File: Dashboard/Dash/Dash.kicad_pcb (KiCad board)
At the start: 2 copper layers, 184 x 75 mm, 43 parts, among them IC1 MCP25625-E_SS, J1 TACH-SERVO, J2 SPEED-SERVO, J6 LOWER Button, J7 DTF13-6P, U1 XIAO-ESP32-S3-SMD, U3 EA DOGM128W-6, Y1 ABM10AIG-16.000MHZ-4Z-T3

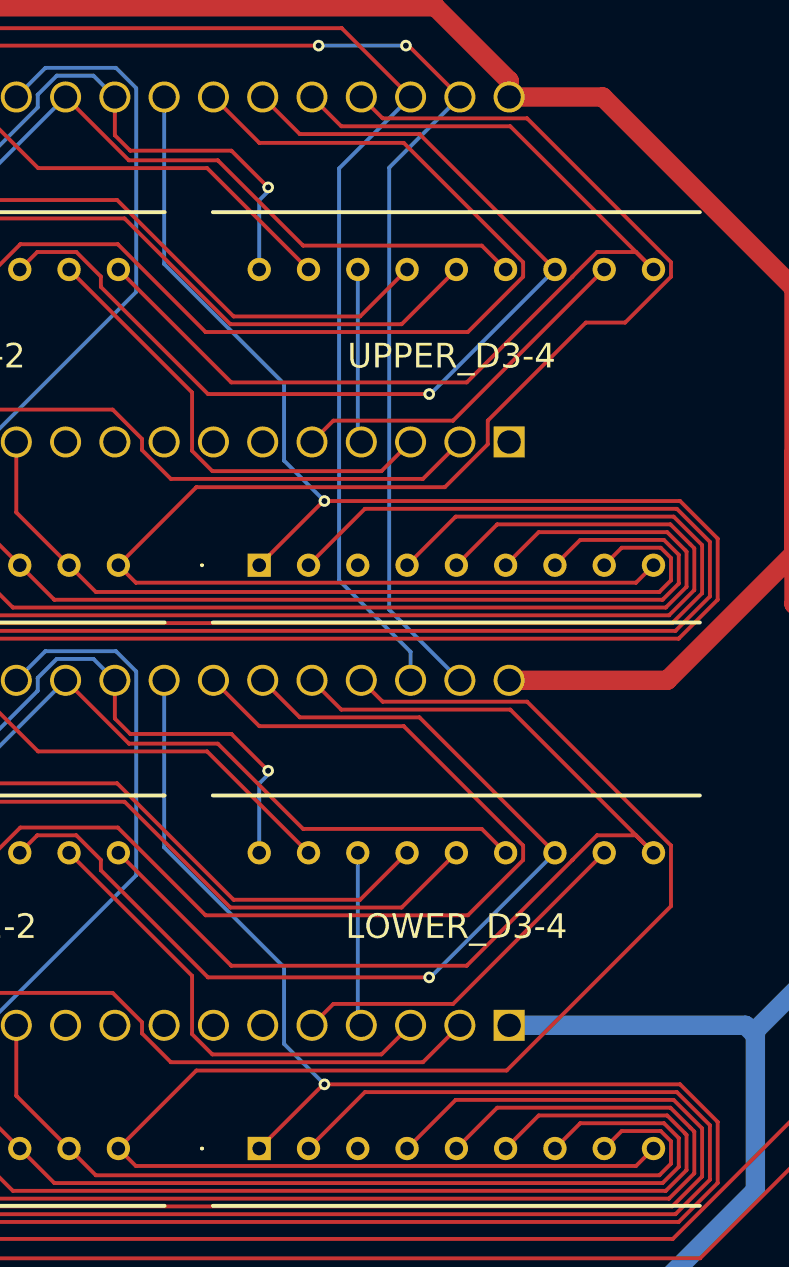
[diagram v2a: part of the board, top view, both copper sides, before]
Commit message: Fixed Shorting DRC Errors
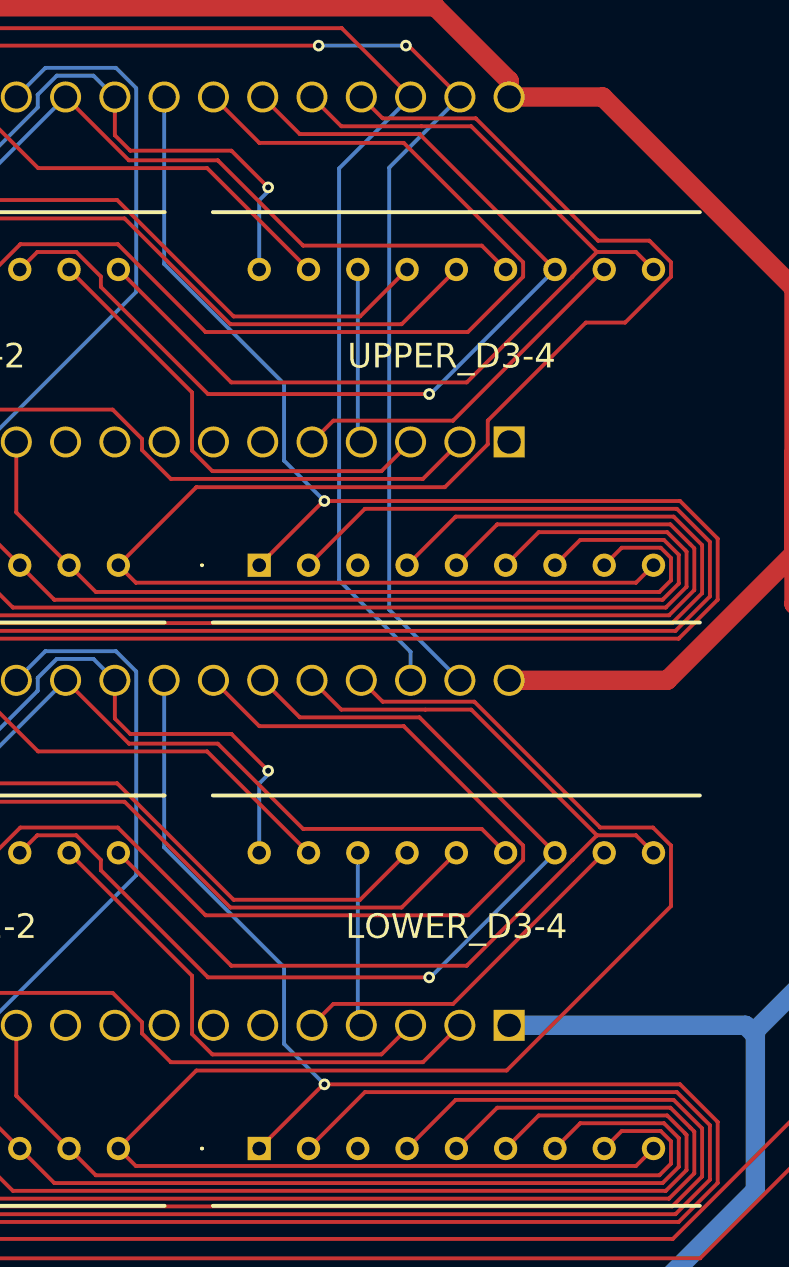
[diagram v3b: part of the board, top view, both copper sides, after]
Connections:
- LOWER_D1-2 pad 8: ROW14_UPPER -> ROW14_LOWER
- LOWER_D3-4 pad 8: ROW14_UPPER -> ROW14_LOWER
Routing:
- net ROW14_LOWER: track 0.00 -> 44.5 mm
- net (no net): track 44.5 -> 0.00 mm
- net ROW1_UPPER: track 54.4 -> 51.1 mm
- net ROW1_LOWER: track 54.4 -> 51.1 mm
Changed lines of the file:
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@@
 			(layers "*.Cu" "*.Mask")
 			(remove_unused_layers no)
-			(net 3 "ROW14_UPPER")
+			(net 15 "ROW14_LOWER")
 			(pinfunction "A_DP")
 			(pintype "passive")
@@
 			(layers "*.Cu" "*.Mask")
 			(remove_unused_layers no)
-			(net 3 "ROW14_UPPER")
+			(net 15 "ROW14_LOWER")
 			(pinfunction "A_DP")
 			(pintype "passive")
@@
 	)
 	(segment
-		(start 181.020325 125.22)
-		(end 210.061325 125.22)
-		(width 0.2)
-		(layer "F.Cu")
-		(net 0)
-	)
-	(segment
-		(start 208.121325 122.939)
-		(end 207.220325 123.84)
-		(width 0.2)
-		(layer "F.Cu")
-		(net 0)
-	)
-	(segment
-		(start 176.920325 117.49)
-		(end 176.920325 121.12)
-		(width 0.2)
-		(layer "F.Cu")
-		(net 0)
-	)
-	(segment
-		(start 176.920325 121.12)
-		(end 181.020325 125.22)
-		(width 0.2)
-		(layer "F.Cu")
-		(net 0)
-	)
-	(segment
-		(start 210.661325 124.62)
-		(end 210.661325 123.466793)
-		(width 0.2)
-		(layer "F.Cu")
-		(net 0)
-	)
-	(segment
-		(start 210.661325 123.466793)
-		(end 210.133532 122.939)
-		(width 0.2)
-		(layer "F.Cu")
-		(net 0)
-	)
-	(segment
-		(start 210.133532 122.939)
-		(end 208.121325 122.939)
-		(width 0.2)
-		(layer "F.Cu")
-		(net 0)
-	)
-	(segment
-		(start 210.061325 125.22)
-		(end 210.661325 124.62)
-		(width 0.2)
-		(layer "F.Cu")
-		(net 0)
-	)
-	(segment
 		(start 181.020325 95.157844)
 		(end 210.061325 95.157844)
@@
 	)
 	(segment
-		(start 193.670325 101.22)
-		(end 202.380325 101.22)
+		(start 209.760325 108.599999)
+		(end 209.760325 108.6)
 		(width 0.2)
 		(layer "F.Cu")
@@
 	)
 	(segment
-		(start 202.380325 101.22)
-		(end 209.760325 108.6)
+		(start 200.134532 114.42)
+		(end 188.000325 114.42)
 		(width 0.2)
 		(layer "F.Cu")
@@
 	)
 	(segment
-		(start 200.134532 114.42)
-		(end 188.000325 114.42)
+		(start 200.368118 101.22)
+		(end 206.847118 107.699)
 		(width 0.2)
 		(layer "F.Cu")
@@
 	)
 	(segment
+		(start 198 101.22)
+		(end 200.368118 101.22)
+		(width 0.2)
+		(layer "F.Cu")
+		(net 7)
+	)
+	(segment
 		(start 192.160325 99.71)
 		(end 193.670325 101.22)
@@
 	)
 	(segment
+		(start 193.670325 101.22)
+		(end 198 101.22)
+		(width 0.2)
+		(layer "F.Cu")
+		(net 7)
+	)
+	(segment
 		(start 183.400325 117.90705)
 		(end 183.400325 117.33295)
@@
 	)
 	(segment
+		(start 181.020325 125.22)
+		(end 210.061325 125.22)
+		(width 0.2)
+		(layer "F.Cu")
+		(net 15)
+	)
+	(segment
+		(start 176.920325 117.49)
+		(end 176.920325 121.12)
+		(width 0.2)
+		(layer "F.Cu")
+		(net 15)
+	)
+	(segment
+		(start 176.920325 121.12)
+		(end 181.020325 125.22)
+		(width 0.2)
+		(layer "F.Cu")
+		(net 15)
+	)
+	(segment
+		(start 210.661325 124.62)
+		(end 210.661325 123.466793)
+		(width 0.2)
+		(layer "F.Cu")
+		(net 15)
+	)
+	(segment
+		(start 210.661325 123.466793)
+		(end 210.133532 122.939)
+		(width 0.2)
+		(layer "F.Cu")
+		(net 15)
+	)
+	(segment
+		(start 208.121325 122.939)
+		(end 207.220325 123.84)
+		(width 0.2)
+		(layer "F.Cu")
+		(net 15)
+	)
+	(segment
+		(start 210.133532 122.939)
+		(end 208.121325 122.939)
+		(width 0.2)
+		(layer "F.Cu")
+		(net 15)
+	)
+	(segment
+		(start 210.061325 125.22)
+		(end 210.661325 124.62)
+		(width 0.2)
+		(layer "F.Cu")
+		(net 15)
+	)
+	(segment
 		(start 207.220325 108.6)
 		(end 199.431325 116.389)
@@
 	)
 	(segment
-		(start 210.661325 111.351)
+		(start 209.732532 107.298)
 		(end 210.661325 108.226793)
 		(width 0.2)
@@
 	)
 	(segment
-		(start 202.192325 119.82)
-		(end 210.661325 111.351)
+		(start 194.700325 99.71)
+		(end 195.801325 100.811)
 		(width 0.2)
 		(layer "F.Cu")
@@
 	)
 	(segment
-		(start 186.200325 119.82)
+		(start 195.801325 100.811)
+		(end 200.526218 100.811)
+		(width 0.2)
+		(layer "F.Cu")
+		(net 44)
+	)
+	(segment
+		(start 210.661325 111.351)
 		(end 202.192325 119.82)
 		(width 0.2)
@@
 	)
 	(segment
-		(start 203.245532 100.811)
-		(end 195.801325 100.811)
+		(start 210.661325 108.226793)
+		(end 210.661325 111.351)
 		(width 0.2)
 		(layer "F.Cu")
@@
 	)
 	(segment
-		(start 182.180325 123.84)
-		(end 186.200325 119.82)
+		(start 207.013218 107.298)
+		(end 209.732532 107.298)
 		(width 0.2)
 		(layer "F.Cu")
@@
 	)
 	(segment
-		(start 208.859325 124.741)
-		(end 209.760325 123.84)
+		(start 186.200325 119.82)
+		(end 182.180325 123.84)
 		(width 0.2)
 		(layer "F.Cu")
@@
 	)
 	(segment
-		(start 195.801325 100.811)
-		(end 194.700325 99.71)
+		(start 202.192325 119.82)
+		(end 186.200325 119.82)
 		(width 0.2)
 		(layer "F.Cu")
@@
 	)
 	(segment
-		(start 182.180325 123.84)
-		(end 183.081325 124.741)
+		(start 208.859325 124.741)
+		(end 209.760325 123.84)
 		(width 0.2)
 		(layer "F.Cu")
@@
 	)
 	(segment
-		(start 210.661325 108.226793)
-		(end 203.245532 100.811)
+		(start 200.526218 100.811)
+		(end 207.013218 107.298)
+		(width 0.2)
+		(layer "F.Cu")
+		(net 44)
+	)
+	(segment
+		(start 182.180325 123.84)
+		(end 183.081325 124.741)
 		(width 0.2)
 		(layer "F.Cu")
@@
 	(segment
 		(start 210.661325 78.164637)
-		(end 203.245532 70.748844)
+		(end 209.548344 77.051656)
+		(width 0.2)
+		(layer "F.Cu")
+		(net 85)
+	)
+	(segment
+		(start 209.548344 77.051656)
+		(end 206.902812 77.051656)
 		(width 0.2)
 		(layer "F.Cu")
@@
 	)
 	(segment
-		(start 203.245532 70.748844)
+		(start 200.6 70.748844)
 		(end 195.801325 70.748844)
 		(width 0.2)
@@
 	)
 	(segment
+		(start 206.902812 77.051656)
+		(end 200.6 70.748844)
+		(width 0.2)
+		(layer "F.Cu")
+		(net 85)
+	)
+	(segment
 		(start 201.219325 86.326844)
 		(end 206.273084 81.273084)
@@
 	)
 	(segment
-		(start 202.380325 71.157844)
-		(end 209.760325 78.537844)
-		(width 0.2)
-		(layer "F.Cu")
-		(net 101)
-	)
-	(segment
 		(start 188.000325 84.357844)
 		(end 182.180325 78.537844)
@@
 	)
 	(segment
+		(start 200.368118 71.157844)
+		(end 206.847118 77.636844)
+		(width 0.2)
+		(layer "F.Cu")
+		(net 101)
+	)
+	(segment
+		(start 197.8 71.157844)
+		(end 200.368118 71.157844)
+		(width 0.2)
+		(layer "F.Cu")
+		(net 101)
+	)
+	(segment
 		(start 205.581325 78.902637)
 		(end 205.581325 78.911051)
@@
 	(segment
 		(start 193.670325 71.157844)
-		(end 202.380325 71.157844)
+		(end 197.8 71.157844)
 		(width 0.2)
 		(layer "F.Cu")

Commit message: I swear the CAN_GND can be safely shorted to GND
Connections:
- IC1 pad 26: CAN_GND -> GND
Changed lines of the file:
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@@
 	(net 105 "unconnected-(UPPER_D3-4-NO_CONNECTED-Pad3)")
 	(net 106 "GND")
-	(net 107 "CAN_GND")
-	(net 108 "unconnected-(PS2-CTRL-Pad3)")
-	(net 109 "unconnected-(PS2-NC_1-Pad5)")
-	(net 110 "unconnected-(PS2-NC_2-Pad8)")
+	(net 107 "unconnected-(PS2-CTRL-Pad3)")
+	(net 108 "unconnected-(PS2-NC_1-Pad5)")
+	(net 109 "unconnected-(PS2-NC_2-Pad8)")
 	(footprint "MCP25625 - SSOP NEW CAN:SOP65P780X200-28N"
 		(layer "F.Cu")
@@
 			(size 0.45 1.8)
 			(layers "F.Cu" "F.Mask" "F.Paste")
-			(net 107 "CAN_GND")
+			(net 106 "GND")
 			(pinfunction "VSS")
 			(pintype "passive")
@@
 			(layers "*.Cu" "*.Mask")
 			(remove_unused_layers no)
-			(net 108 "unconnected-(PS2-CTRL-Pad3)")
+			(net 107 "unconnected-(PS2-CTRL-Pad3)")
 			(pinfunction "CTRL")
 			(pintype "passive+no_connect")
@@
 			(layers "*.Cu" "*.Mask")
 			(remove_unused_layers no)
-			(net 109 "unconnected-(PS2-NC_1-Pad5)")
+			(net 108 "unconnected-(PS2-NC_1-Pad5)")
 			(pinfunction "NC_1")
 			(pintype "passive+no_connect")
@@
 			(layers "*.Cu" "*.Mask")
 			(remove_unused_layers no)
-			(net 110 "unconnected-(PS2-NC_2-Pad8)")
+			(net 109 "unconnected-(PS2-NC_2-Pad8)")
 			(pinfunction "NC_2")
 			(pintype "passive+no_connect")

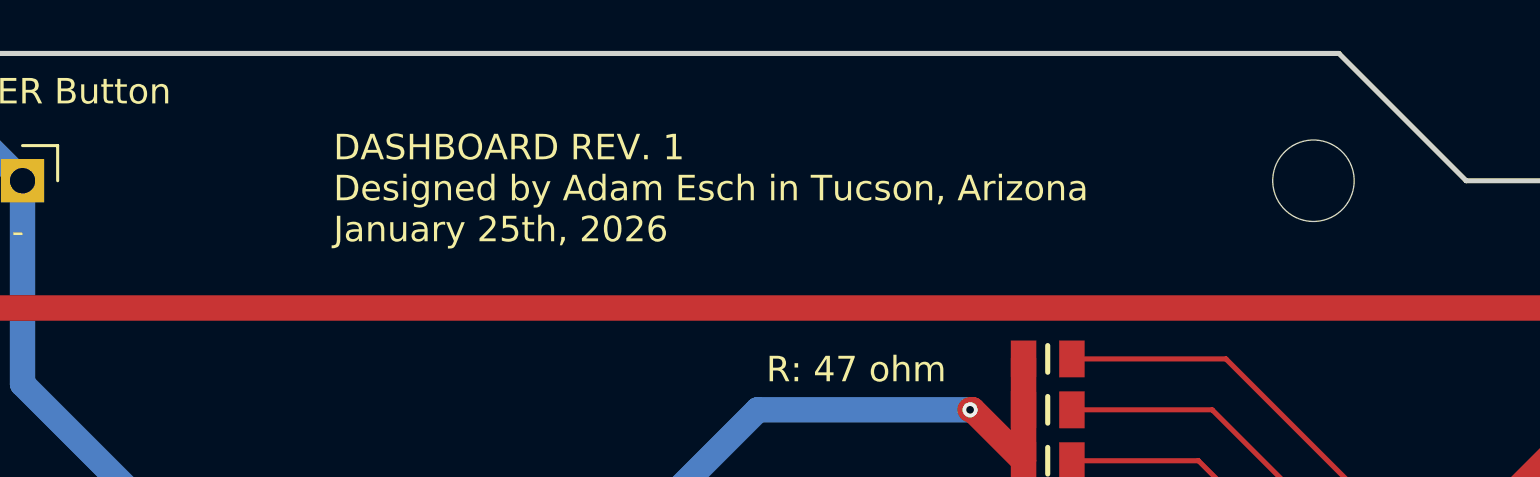
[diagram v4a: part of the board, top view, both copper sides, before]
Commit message: Fixed Schematic and Removed CAN_GND on CAN chip
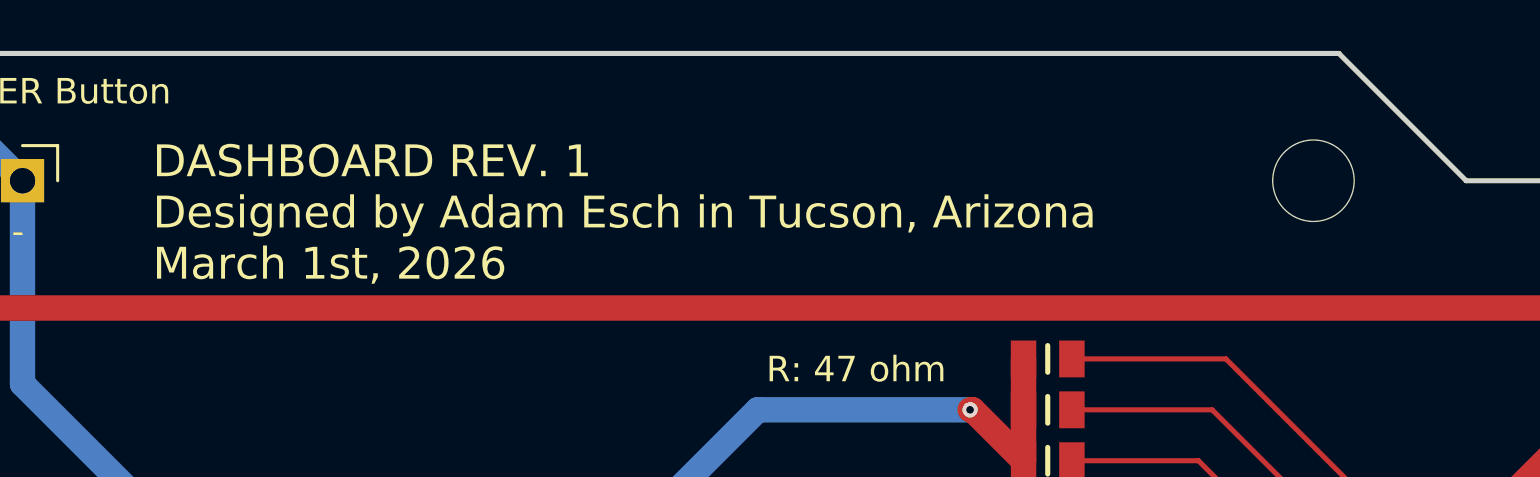
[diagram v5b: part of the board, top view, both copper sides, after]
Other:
- board text added: "DASHBOARD REV. 1 Designed by Adam Esch in Tucson, Arizona March 1st, 2026"
- board text removed: "DASHBOARD REV. 1 Designed by Adam Esch in Tucson, Arizona January 25th, 2026"
